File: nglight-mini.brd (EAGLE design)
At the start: 15.6 x 19.4 mm, 25 parts, among them X1 53261-04

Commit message: Minor changes
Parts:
- C2: device rcl:C1206 -> rcl:UD-4X5,8_NICHICON
- moved C1 0.63 mm to (2.54, 7.94)
- moved C2 0.51 mm to (4.60, 7.18), turned to 270 degrees
- renumbered X1 to I2C
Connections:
- net +5V: now also C2.+; no longer C2.1
- net GND: now also C2.-; no longer C2.2
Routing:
- net N$11: track 7.29 -> 7.85 mm
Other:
- board text removed: "LED GND"

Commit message: Ground unused array resistors
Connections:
- net GND: now also RN2.3, RN2.4, RN2.5, RN2.6, RN4.3, RN4.4, RN4.5, RN4.6
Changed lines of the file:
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@@
 <via x="13.0175" y="12.065" extent="1-16" drill="0.3302"/>
 <via x="12.7" y="4.7625" extent="1-16" drill="0.3302"/>
+<contactref element="RN2" pad="3"/>
+<contactref element="RN2" pad="4"/>
+<contactref element="RN4" pad="6"/>
+<contactref element="RN4" pad="5"/>
+<contactref element="RN2" pad="5"/>
+<contactref element="RN4" pad="4"/>
+<contactref element="RN2" pad="6"/>
+<contactref element="RN4" pad="3"/>
 </signal>
 <signal name="N$2">

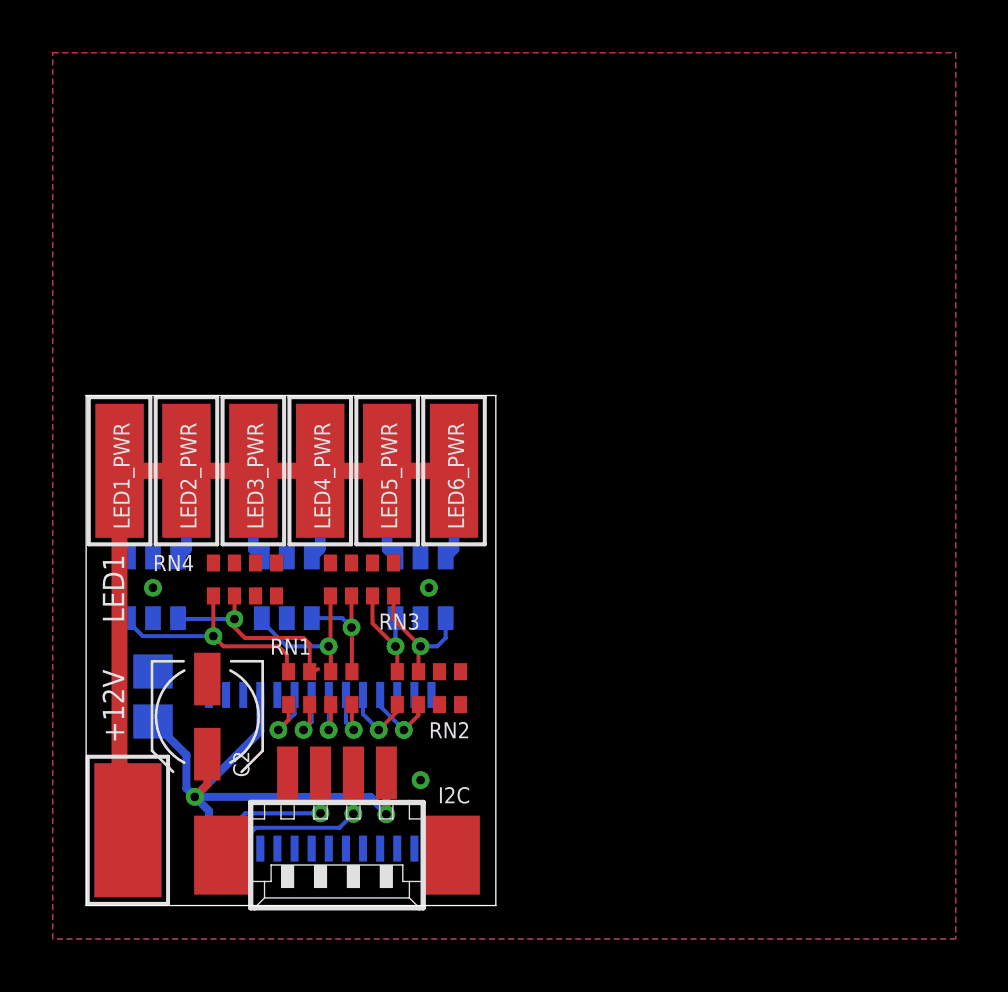
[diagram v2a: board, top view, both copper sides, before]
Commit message: Rev 1; various small improvements, incl.:
- bigger traces (6 mil -> 10 mil)
- larger footprint for the big cap
- remove a small piece of trace between two pins
  that wasn't supposed to be there
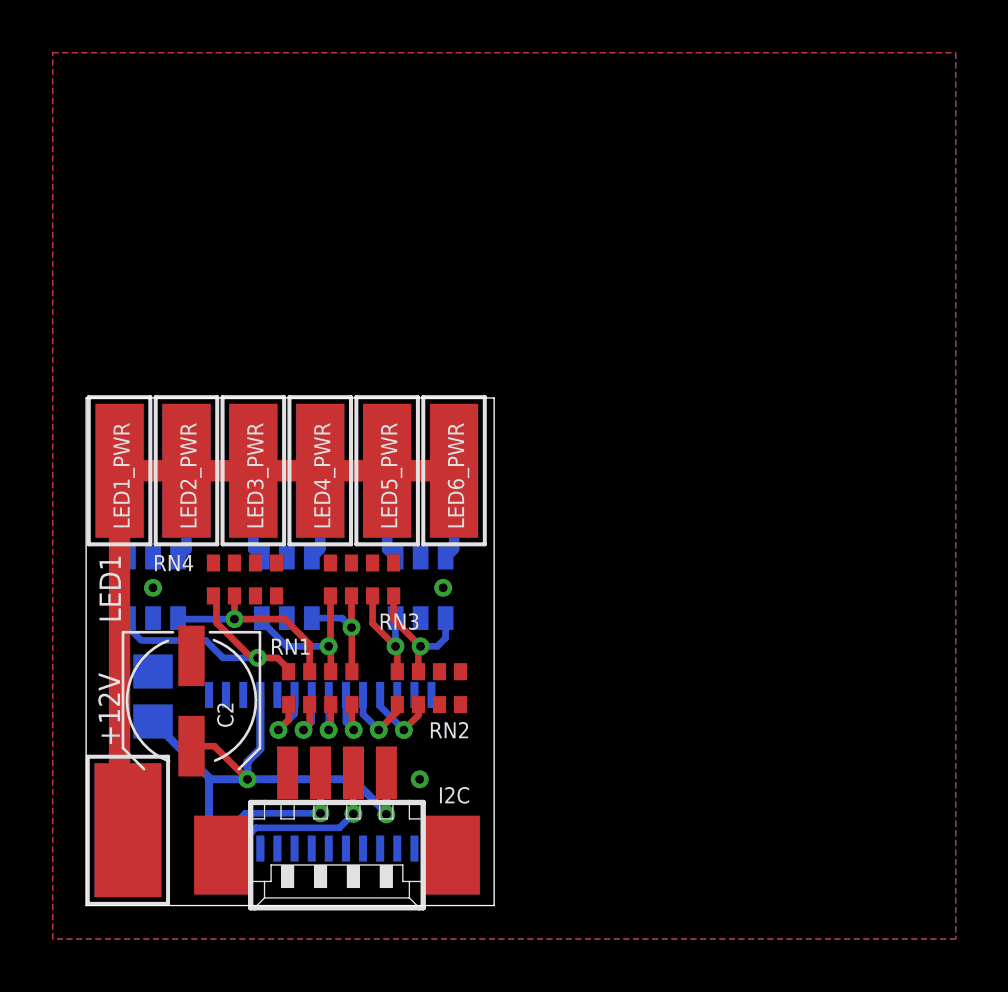
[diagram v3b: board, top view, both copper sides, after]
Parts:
- C2: device rcl:UD-4X5,8_NICHICON -> rcl:UD-5X5,8_NICHICON
- moved C2 0.85 mm to (4.00, 7.78)
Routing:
- net N$9: track 8.88 -> 10.8 mm
- net +5V: track 21.6 -> 20.7 mm
- net N$11: track 7.85 -> 7.34 mm
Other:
- board size 15.6 x 19.4 mm -> 15.5 x 19.3 mm
- board text added: "nglight-mini r1"
- board text removed: "nglight-mini r0"

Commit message: Major changes in layout
The resistor arrays proved hard to solder, so I increased
the pad size. Due to the tight space constraints, this led
to relatively big changes in the board. One consequence is
that traces are now 8mil - a compromise between the 6mil
that seemed too fine and the 10mil that just wont fit.
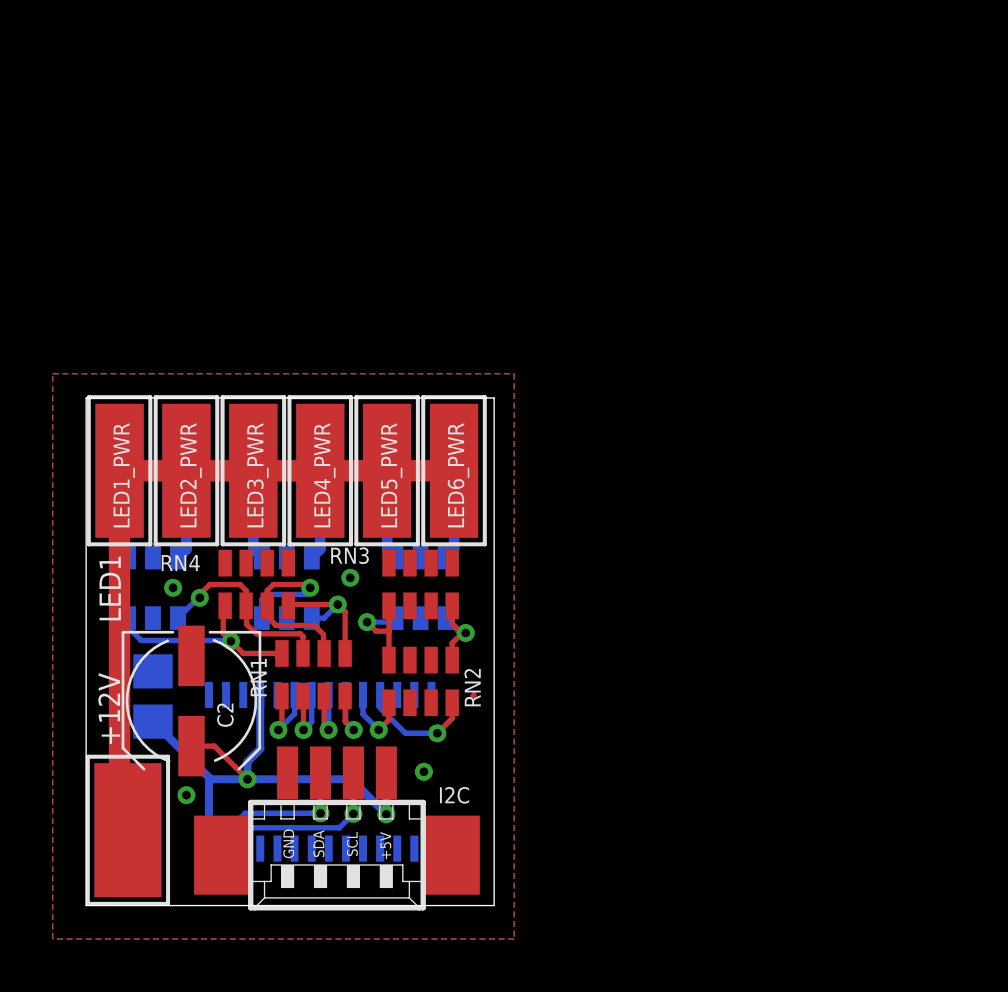
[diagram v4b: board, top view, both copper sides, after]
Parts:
- RN1, RN2: value 240 -> 220R; device resistor-dil:0603-ARC -> r0603array:0603_ARRAY_4
- RN3, RN4: device resistor-dil:0603-ARC -> r0603array:0603_ARRAY_4
- moved RN3 2.23 mm to (12.7, 12.2)
- moved RN1 0.57 mm to (8.64, 8.76)
- moved RN4 0.48 mm to (6.48, 12.2)
- moved RN2 0.41 mm to (12.7, 8.51)
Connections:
- net LED6 renamed N$1
- net GND: now also RN2.2, RN2.7, RN3.2, RN3.3; no longer RN2.4, RN2.5, RN4.3, RN4.4
- net N$2: now also RN3.1; no longer RN3.3
- net N$4: now also RN2.5; no longer RN2.7
- net N$6: now also RN4.3; no longer RN3.1
- net N$8: now also RN4.4; no longer RN3.2
- net PWM6: now also RN2.4; no longer RN2.2
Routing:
- net N$6: track 5.99 -> 9.30 mm
- net N$9: track 10.8 -> 8.65 mm
- net PWM6: track 2.89 -> 4.46 mm
- net N$4: track 5.18 -> 3.65 mm
- net N$8: track 4.54 -> 5.07 mm
- net PWM4: track 2.44 -> 2.97 mm
- net GND: track 0.00 -> 0.07 mm, vias 3 -> 4
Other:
- board text added: "+5V"
- board text added: "GND"
- board text added: "SCL"
- board text added: "SDA"
